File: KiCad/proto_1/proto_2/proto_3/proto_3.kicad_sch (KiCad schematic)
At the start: 12 parts

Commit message: KiCad/proto_1/proto_2/proto_3/proto_3.kicad_pcb
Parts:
- removed L2: ~, Inductor-4.7uH-60ohm:IND_BOURNS_RLB9012, symbol Inductor-4.7uH/60ohm:RLB9012-4R7ML
- added L1: RLB9012-4R7ML, stuff:IND_RLB9012-4R7ML, symbol Inductor-4.7uH/60ohm:RLB9012-4R7ML
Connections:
- net at C3.1, C4.1, J1.1: now also L1.1
- net at C2.1, U1.6 (+Vo): now also L1.2
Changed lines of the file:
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@@
-	)
-	(symbol
-		(lib_id "Inductor-4.7uH/60ohm:RLB9012-4R7ML")
-		(at 161.29 102.87 0)
-		(unit 1)
-		(exclude_from_sim no)
-		(in_bom yes)
-		(on_board yes)
-		(dnp no)
-		(fields_autoplaced yes)
-		(property "Reference" "L2"
-			(at 168.91 96.52 0)
-			(effects
-				(font
-					(size 1.524 1.524)
-				)
-			)
-		)
-		(property "Value" "~"
-			(at 168.91 99.06 0)
-			(effects
-				(font
-					(size 1.524 1.524)
-				)
-			)
-		)
-		(property "Footprint" "Inductor-4.7uH-60ohm:IND_BOURNS_RLB9012"
-			(at 161.29 102.87 0)
-			(effects
-				(font
-					(size 1.27 1.27)
-					(italic yes)
-				)
-				(hide yes)
-			)
-		)
-		(property "Datasheet" "RLB9012-4R7ML"
-			(at 161.29 102.87 0)
-			(effects
-				(font
-					(size 1.27 1.27)
-					(italic yes)
-				)
-				(hide yes)
-			)
-		)
-		(property "Description" ""
-			(at 161.29 102.87 0)
-			(effects
-				(font
-					(size 1.27 1.27)
-				)
-				(hide yes)
-			)
-		)
-		(pin "2"
-		)
-		(pin "1"
-		)
-		(instances
-			(project ""
-				(path "/3ba3c426-0aff-4728-abf4-4c9cd318aec8"
-					(reference "L2")
-					(unit 1)
-				)
-			)
-		)
 	)
 	(symbol
@@
 					(unit 1)
 				)
+			)
+		)
+	)
+	(symbol
+		(lib_id "Inductor-4.7uH/60ohm:RLB9012-4R7ML")
+		(at 161.29 102.87 0)
+		(unit 1)
+		(exclude_from_sim no)
+		(in_bom yes)
+		(on_board yes)
+		(dnp no)
+		(fields_autoplaced yes)
+		(property "Reference" "L1"
+			(at 168.91 95.25 0)
+			(effects
+				(font
+					(size 1.524 1.524)
+				)
+			)
+		)
+		(property "Value" "RLB9012-4R7ML"
+			(at 168.91 97.79 0)
+			(effects
+				(font
+					(size 1.524 1.524)
+				)
+			)
+		)
+		(property "Footprint" "stuff:IND_RLB9012-4R7ML"
+			(at 161.29 102.87 0)
+			(effects
+				(font
+					(size 1.27 1.27)
+					(italic yes)
+				)
+				(hide yes)
+			)
+		)
+		(property "Datasheet" "RLB9012-4R7ML"
+			(at 161.29 102.87 0)
+			(effects
+				(font
+					(size 1.27 1.27)
+					(italic yes)
+				)
+				(hide yes)
+			)
+		)
+		(property "Description" ""
+			(at 161.29 102.87 0)
+			(effects
+				(font
+					(size 1.27 1.27)
+				)
+				(hide yes)
+			)
+		)
+		(pin "1"
+		)
+		(pin "2"
+		)
+		(instances
+			(project ""
+				(path "/3ba3c426-0aff-4728-abf4-4c9cd318aec8"
+					(reference "L1")
+					(unit 1)
+				)

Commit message: Added correct LDM inductor, footprint and symbol
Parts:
- removed LDM1: ~, Inductor-4.7uH-60ohm:IND_BOURNS_RLB9012, symbol Inductor-4.7uH/60ohm:RLB9012-4R7ML
- added LDM: ~, AIUR-06_ABR, symbol 4.7mHInductor:AIUR-06-472K
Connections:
- net at U1.1 (AC(L)): now also LDM.1
- net at R1.2: now also LDM.2
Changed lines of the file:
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@@
+	)
+	(junction
+		(at 113.03 102.87)
+		(diameter 0)
+		(color 0 0 0 0)
 	)
 	(junction
@@
 	)
 	(junction
-		(at 113.03 102.87)
-		(diameter 0)
-		(color 0 0 0 0)
-	)
-	(junction
 		(at 180.34 111.76)
 		(diameter 0)
@@
 	(wire
 		(pts
-			(xy 113.03 102.87) (xy 107.95 102.87)
+			(xy 107.95 102.87) (xy 113.03 102.87)
 		)
 		(stroke
@@
 	(wire
 		(pts
-			(xy 114.3 102.87) (xy 113.03 102.87)
-		)
-		(stroke
-			(width 0)
-			(type default)
-		)
-	)
-	(wire
-		(pts
 			(xy 66.04 114.3) (xy 66.04 135.89)
 		)
@@
 	(wire
 		(pts
+			(xy 113.03 102.87) (xy 114.3 102.87)
+		)
+		(stroke
+			(width 0)
+			(type default)
+		)
+	)
+	(wire
+		(pts
 			(xy 186.69 102.87) (xy 195.58 102.87)
 		)
@@
 	)
 	(symbol
-		(lib_id "Inductor-4.7uH/60ohm:RLB9012-4R7ML")
+		(lib_id "4.7mHInductor:AIUR-06-472K")
 		(at 113.03 102.87 0)
 		(unit 1)
@@
 		(dnp no)
 		(fields_autoplaced yes)
-		(property "Reference" "LDM1"
+		(property "Reference" "LDM"
 			(at 120.65 96.52 0)
 			(effects
@@
 			)
 		)
-		(property "Footprint" "Inductor-4.7uH-60ohm:IND_BOURNS_RLB9012"
+		(property "Footprint" "AIUR-06_ABR"
 			(at 113.03 102.87 0)
 			(effects
@@
 			)
 		)
-		(property "Datasheet" "RLB9012-4R7ML"
+		(property "Datasheet" "AIUR-06-472K"
 			(at 113.03 102.87 0)
 			(effects
@@
 			)
 		)
+		(pin "1"
+		)
 		(pin "2"
 		)
-		(pin "1"
-		)
 		(instances
-			(project "proto_3"
+			(project ""
 				(path "/3ba3c426-0aff-4728-abf4-4c9cd318aec8"
-					(reference "LDM1")
+					(reference "LDM")
 					(unit 1)
 				)

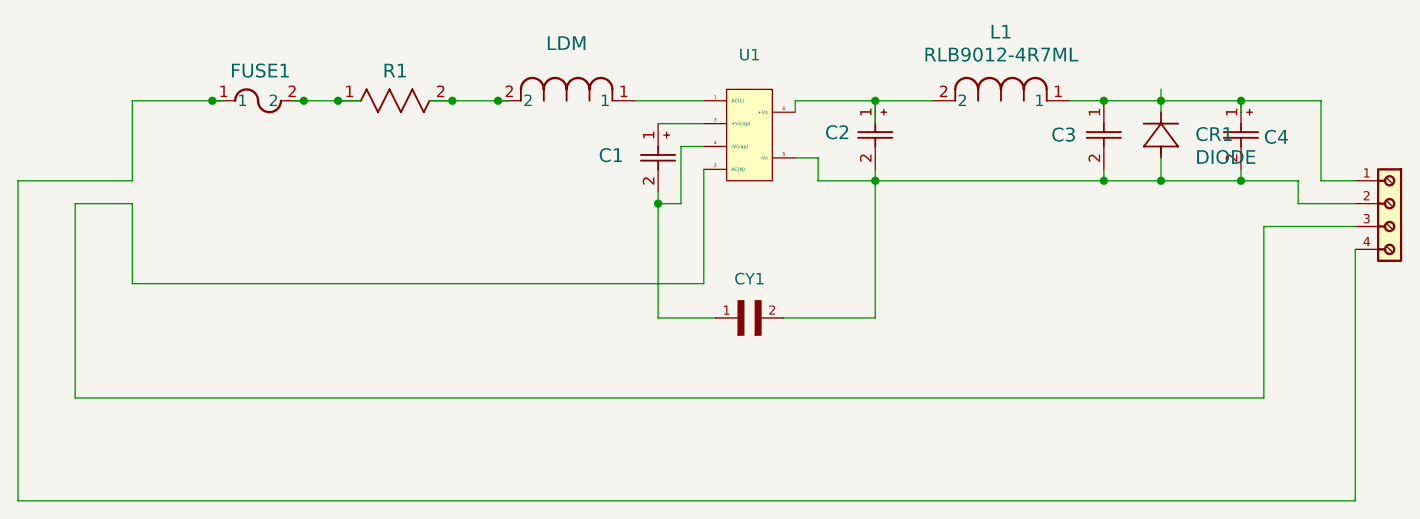
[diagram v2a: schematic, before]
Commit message: Added correct TVS diode footprint with correct polarities.
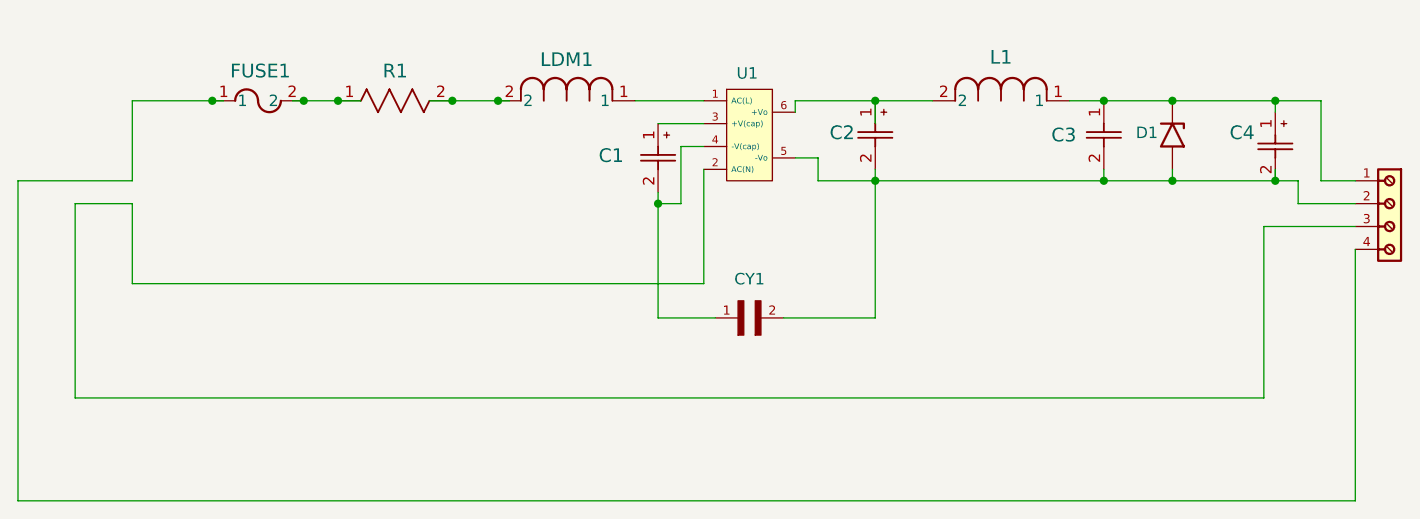
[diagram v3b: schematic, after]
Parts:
- removed CR1: DIODE, stuff:SMBJ7.0A, symbol SMBJ-7A:DIODE
- added D1: SM6T6V8A, stuff:TVS_DIODE_NEW, symbol Diode:SM6T6V8A
- L1: value RLB9012-4R7ML -> ~
- renumbered LDM to LDM1
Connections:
- net at C3.1, C4.1, J1.1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: now also D1.1 (A1)
- net at C2.2, C3.2, C4.2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: now also D1.2 (A2)
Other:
- moved on the sheet: C4
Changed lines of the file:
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@@
 	(paper "A4")
 	(junction
-		(at 195.58 102.87)
+		(at 187.96 102.87)
 		(diameter 0)
 		(color 0 0 0 0)
@@
 	)
 	(junction
-		(at 186.69 111.76)
+		(at 187.96 111.76)
 		(diameter 0)
 		(color 0 0 0 0)
@@
 	)
 	(junction
-		(at 186.69 102.87)
-		(diameter 0)
-		(color 0 0 0 0)
-	)
-	(junction
 		(at 113.03 102.87)
 		(diameter 0)
@@
 	)
 	(junction
-		(at 195.58 111.76)
+		(at 199.39 111.76)
+		(diameter 0)
+		(color 0 0 0 0)
+	)
+	(junction
+		(at 199.39 102.87)
 		(diameter 0)
 		(color 0 0 0 0)
@@
 	(wire
 		(pts
+			(xy 187.96 111.76) (xy 199.39 111.76)
+		)
+		(stroke
+			(width 0)
+			(type default)
+		)
+	)
+	(wire
+		(pts
 			(xy 133.35 107.95) (xy 133.35 114.3)
 		)
@@
 	(wire
 		(pts
+			(xy 187.96 102.87) (xy 199.39 102.87)
+		)
+		(stroke
+			(width 0)
+			(type default)
+		)
+	)
+	(wire
+		(pts
 			(xy 72.39 102.87) (xy 72.39 111.76)
 		)
@@
 	(wire
 		(pts
-			(xy 186.69 111.76) (xy 195.58 111.76)
+			(xy 187.96 110.49) (xy 187.96 111.76)
 		)
 		(stroke
@@
 	(wire
 		(pts
+			(xy 199.39 110.49) (xy 199.39 111.76)
+		)
+		(stroke
+			(width 0)
+			(type default)
+		)
+	)
+	(wire
+		(pts
 			(xy 154.94 102.87) (xy 154.94 105.41)
 		)
@@
 	(wire
 		(pts
-			(xy 186.69 102.87) (xy 186.69 104.14)
+			(xy 199.39 111.76) (xy 201.93 111.76)
 		)
 		(stroke
@@
 	(wire
 		(pts
-			(xy 195.58 111.76) (xy 201.93 111.76)
-		)
-		(stroke
-			(width 0)
-			(type default)
-		)
-	)
-	(wire
-		(pts
 			(xy 113.03 102.87) (xy 114.3 102.87)
 		)
@@
 	(wire
 		(pts
-			(xy 186.69 102.87) (xy 195.58 102.87)
-		)
-		(stroke
-			(width 0)
-			(type default)
-		)
-	)
-	(wire
-		(pts
 			(xy 72.39 123.19) (xy 72.39 114.3)
 		)
@@
 	(wire
 		(pts
-			(xy 195.58 102.87) (xy 195.58 104.14)
-		)
-		(stroke
-			(width 0)
-			(type default)
-		)
-	)
-	(wire
-		(pts
 			(xy 130.81 127) (xy 137.16 127)
 		)
@@
 	(wire
 		(pts
+			(xy 180.34 102.87) (xy 187.96 102.87)
+		)
+		(stroke
+			(width 0)
+			(type default)
+		)
+	)
+	(wire
+		(pts
 			(xy 107.95 102.87) (xy 105.41 102.87)
 		)
@@
 	(wire
 		(pts
-			(xy 180.34 102.87) (xy 186.69 102.87)
+			(xy 199.39 102.87) (xy 199.39 104.14)
 		)
 		(stroke
@@
 	(wire
 		(pts
-			(xy 186.69 109.22) (xy 186.69 111.76)
-		)
-		(stroke
-			(width 0)
-			(type default)
-		)
-	)
-	(wire
-		(pts
 			(xy 148.59 109.22) (xy 148.59 111.76)
 		)
@@
 	(wire
 		(pts
-			(xy 195.58 102.87) (xy 204.47 102.87)
-		)
-		(stroke
-			(width 0)
-			(type default)
-		)
-	)
-	(wire
-		(pts
 			(xy 59.69 111.76) (xy 72.39 111.76)
 		)
@@
 	(wire
 		(pts
-			(xy 180.34 111.76) (xy 186.69 111.76)
+			(xy 180.34 111.76) (xy 187.96 111.76)
 		)
 		(stroke
@@
 	(wire
 		(pts
-			(xy 195.58 110.49) (xy 195.58 111.76)
-		)
-		(stroke
-			(width 0)
-			(type default)
-		)
-	)
-	(wire
-		(pts
 			(xy 204.47 102.87) (xy 204.47 111.76)
 		)
@@
 	(wire
 		(pts
-			(xy 186.69 101.6) (xy 186.69 102.87)
+			(xy 199.39 102.87) (xy 204.47 102.87)
 		)
 		(stroke
@@
 		(on_board yes)
 		(dnp no)
-		(fields_autoplaced yes)
-		(property "Reference" "LDM"
-			(at 120.65 96.52 0)
+		(property "Reference" "LDM1"
+			(at 120.65 98.298 0)
 			(effects
 				(font
@@
 			(project ""
 				(path "/3ba3c426-0aff-4728-abf4-4c9cd318aec8"
-					(reference "LDM")
+					(reference "LDM1")
+					(unit 1)
+				)
+			)
+		)
+	)
+	(symbol
+		(lib_id "Diode:SM6T6V8A")
+		(at 187.96 106.68 270)
+		(unit 1)
+		(exclude_from_sim no)
+		(in_bom yes)
+		(on_board yes)
+		(dnp no)
+		(property "Reference" "D1"
+			(at 183.896 106.426 90)
+			(effects
+				(font
+					(size 1.27 1.27)
+				)
+				(justify left)
+			)
+		)
+		(property "Value" "SM6T6V8A"
+			(at 190.5 107.9499 90)
+			(effects
+				(font
+					(size 1.27 1.27)
+				)
+				(justify left)
+				(hide yes)
+			)
+		)
+		(property "Footprint" "stuff:TVS_DIODE_NEW"
+			(at 182.88 106.68 0)
+			(effects
+				(font
+					(size 1.27 1.27)
+				)
+				(hide yes)
+			)
+		)
+		(property "Datasheet" "https://www.st.com/resource/en/datasheet/sm6t.pdf"
+			(at 187.96 105.41 0)
+			(effects
+				(font
+					(size 1.27 1.27)
+				)
+				(hide yes)
+			)
+		)
+		(property "Description" "600W unidirectional Transil Transient Voltage Suppressor, 6.8Vrwm, DO-214AA"
+			(at 187.96 106.68 0)
+			(effects
+				(font
+					(size 1.27 1.27)
+				)
+				(hide yes)
+			)
+		)
+		(pin "1"
+		)
+		(pin "2"
+		)
+		(instances
+			(project ""
+				(path "/3ba3c426-0aff-4728-abf4-4c9cd318aec8"
+					(reference "D1")
 					(unit 1)
 				)
@@
 	(symbol
 		(lib_id "Capacitor-.1uf-50v:UFW1H0R1MDD1TA")
-		(at 195.58 102.87 270)
+		(at 199.39 104.14 270)
 		(unit 1)
 		(exclude_from_sim no)
@@
 		(dnp no)
 		(property "Reference" "C4"
-			(at 198.12 106.934 90)
+			(at 194.31 106.426 90)
 			(effects
 				(font
@@
 		)
 		(property "Value" "~"
-			(at 199.39 107.1753 90)
+			(at 203.2 108.4453 90)
 			(effects
 				(font
@@
 		)
 		(property "Footprint" "Capacitor-,1uF-50V:CAP_UEP_5X11_NCH"
-			(at 195.58 102.87 0)
+			(at 199.39 104.14 0)
 			(effects
 				(font
@@
 		)
 		(property "Datasheet" "UFW1H0R1MDD1TA"
-			(at 195.58 102.87 0)
+			(at 199.39 104.14 0)
 			(effects
 				(font
@@
 		)
 		(property "Description" ""
-			(at 195.58 102.87 0)
+			(at 199.39 104.14 0)
 			(effects
 				(font
@@
 		(dnp no)
 		(property "Reference" "C2"
-			(at 152.146 106.426 90)
+			(at 152.654 106.426 90)
 			(effects
 				(font
@@
 		(on_board yes)
 		(dnp no)
-		(fields_autoplaced yes)
 		(property "Reference" "U1"
-			(at 140.97 97.79 0)
+			(at 140.716 99.822 0)
 			(effects
 				(font
@@
 	)
 	(symbol
-		(lib_id "SMBJ-7A:DIODE")
-		(at 186.69 111.76 90)
-		(unit 1)
-		(exclude_from_sim no)
-		(in_bom yes)
-		(on_board yes)
-		(dnp no)
-		(fields_autoplaced yes)
-		(property "Reference" "CR1"
-			(at 190.5 106.6291 90)
-			(effects
-				(font
-					(size 1.524 1.524)
-				)
-				(justify right)
-			)
-		)
-		(property "Value" "DIODE"
-			(at 190.5 109.1691 90)
-			(effects
-				(font
-					(size 1.524 1.524)
-				)
-				(justify right)
-			)
-		)
-		(property "Footprint" "stuff:SMBJ7.0A"
-			(at 195.834 106.68 0)
-			(effects
-				(font
-					(size 1.524 1.524)
-				)
-				(hide yes)
-			)
-		)
-		(property "Datasheet" ""
-			(at 186.69 111.76 0)
-			(effects
-				(font
-					(size 1.524 1.524)
-				)
-			)
-		)
-		(property "Description" ""
-			(at 186.69 111.76 0)
-			(effects
-				(font
-					(size 1.27 1.27)
-				)
-				(hide yes)
-			)
-		)
-		(pin "2"
-		)
-		(pin "1"
-		)
-		(instances
-			(project ""
-				(path "/3ba3c426-0aff-4728-abf4-4c9cd318aec8"
-					(reference "CR1")
-					(unit 1)
-				)
-			)
-		)
-	)
-	(symbol
 		(lib_id "Inductor-4.7uH/60ohm:RLB9012-4R7ML")
 		(at 161.29 102.87 0)
@@
 		(on_board yes)
 		(dnp no)
-		(fields_autoplaced yes)
 		(property "Reference" "L1"
-			(at 168.91 95.25 0)
+			(at 168.91 98.044 0)
 			(effects
 				(font
@@
 			)
 		)
-		(property "Value" "RLB9012-4R7ML"
-			(at 168.91 97.79 0)
-			(effects
-				(font
+		(property "Value" "~"
+			(at 168.91 99.06 0)
+			(effects
+				(font
